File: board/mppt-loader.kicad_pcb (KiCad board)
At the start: 2 copper layers, 102 parts, among them IC101 ATTINY461A-S, IC102 MCP2551-I/SN, P101 CONN_3X2, P102 TST, P103 CONN_11, P104 CONN_11, P105 CONN_5, P106 CONN_4, Q201 IRF 530NS, Q202 IRF 530NS, Q203 IRF 530NS, Q204 IRF 530NS, U101 MCP2515, U102 LD1117-5.0, U201 IR2110, U202 IR2110, U203 LM393, X101 8MHz

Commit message: Finished Schematic and PCB
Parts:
- removed C110, C111: CP, C1V5
- removed U102: LD1117-5.0, SOT223
- added C1: 10u, SM1210, F.Cu at (163.7, 146.0)
- added C2: 10u, SM1210, F.Cu at (163.7, 142.6)
- added C3: 100n, SM0603_Capa, F.Cu at (159.0, 139.8)
- added C4: 10u, SM1210, F.Cu at (168.6, 136.1)
- added C5: 10u, SM1210, F.Cu at (172.0, 136.1)
- added C6: 100n, SM0603_Capa, F.Cu at (171.0, 141.6)
- added C7: 22n, SM0603_Capa, F.Cu at (171.5, 146.8)
- added D1: DIODESCH, DO-214AC(SMA), F.Cu at (164.0, 138.9)
- added F101: FUSE, FUSE5-20, F.Cu at (178.0, 129.1)
- added L1: 22u, SM1210, F.Cu at (163.7, 135.1)
- added R1: 52k3, SM0805, F.Cu at (155.5, 139.1)
- added R2: 10k, SM0805, F.Cu at (155.5, 142.9)
- added R3: 100, SM0805, F.Cu at (175.8, 150.0)
- added R4: 1M, SM0805, F.Cu at (159.2, 146.6)
- added U1: MCP16301, SOT23_6, F.Cu at (159.0, 142.5)
- added U2: LM4132-2.5, SOT23-5, F.Cu at (171.0, 144.2)
- added W102: TEST, PIN_ARRAY_2X1, F.Cu at (165.2, 177.1)
- D102, D103: footprint LED-0805 -> LED-5MM
- D104: value DIODE -> 1N4148; footprint SM1206POL -> sot23
- P103, P104: value CONN_11 -> CONN_12; footprint SIL-12 -> pin_array_6x2
- P105: footprint SIL-5 -> pin_array_3x2
- P106: value CONN_4 -> CONN_8; footprint RIACON_007-4 -> bopla_ak700_8h; moved to B.Cu
- moved C209 177.1 mm to (232.7, 166.7)
- moved C213 176.9 mm to (224.3, 142.2), turned to 180 degrees
- moved C219 174.5 mm to (224.1, 166.9)
- moved Q202 173.5 mm to (223.1, 107.5), turned to 180 degrees
- moved C211 171.2 mm to (232.7, 125.1)
- moved C221 170.7 mm to (224.1, 159.7)
- moved C109 168.7 mm to (177.7, 177.9), turned to 90 degrees
- moved D211 168.0 mm to (229.9, 139.3), turned to 270 degrees
- moved D202 158.0 mm to (205.1, 156.5), turned to 90 degrees
- moved R202 157.7 mm to (223.1, 104.5)
- moved R204 157.6 mm to (223.1, 146.1)
- moved C215 157.2 mm to (228.3, 163.3), turned to 180 degrees
- moved P105 150.0 mm to (172.8, 177.1)
- moved R206 149.4 mm to (200.1, 158.9), turned to 270 degrees
- moved C223 149.2 mm to (219.9, 121.7)
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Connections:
- net N-0000026 renamed /VBAT
- C104 pad 1: N-0000022 (its old number) -> /AVCC
- C107 pad 1: N-0000023 (its old number) -> /VREF
- C203 pad 1: /Powerstage/SENSEA_VOUT -> /Powerstage/VDD_PWR
- C204 pad 1: /Powerstage/SENSEA_VOUT -> /Powerstage/VDD_PWR
- C205 pad 1: /Powerstage/SENSEA_VOUT -> /Powerstage/VDD_PWR
- C206 pad 1: /Powerstage/SENSEA_VOUT -> /Powerstage/VDD_PWR
- C207 pad 2: N-0000074 (its old number) -> /Powerstage/VSA
- C208 pad 2: N-0000066 (its old number) -> /Powerstage/VSB
- C213 pad 2: /Powerstage/SENSEA_VOUT -> /Powerstage/VDD_PWR
- D104 pad 1: /Powerstage/VDD_LOGIC -> +5V
- D104 pad 2: /Powerstage/SENSEA_VOUT -> N-0000032
- D205 pad 1: /Powerstage/SENSEA_VOUT -> /Powerstage/VDD_PWR
- D206 pad 1: /Powerstage/SENSEA_VOUT -> /Powerstage/VDD_PWR
- D207 pad 2: N-0000074 (its old number) -> /Powerstage/VSA
- D208 pad 2: N-0000066 (its old number) -> /Powerstage/VSB
- D209 pad 2: /Powerstage/SENSEA_VOUT -> /Powerstage/VDD_PWR
- D210 pad 2: /Powerstage/SENSEA_VOUT -> /Powerstage/VDD_PWR
- D211 pad 2: /Powerstage/SENSEA_VOUT -> /Powerstage/VDD_PWR
- D212 pad 2: /Powerstage/SENSEA_VOUT -> /Powerstage/VDD_PWR
- IC101 pad 1: N-0000020 (its old number) -> N-0000016
- IC101 pad 15: N-0000022 (its old number) -> /AVCC
- IC101 pad 17: N-0000023 (its old number) -> /VREF
- IC101 pad 19: (no net) -> /CAN_SI
- IC101 pad 2: N-0000011 -> N-0000015
- IC101 pad 3: N-0000019 (its old number) -> N-0000014
- IC101 pad 4: N-0000018 (its old number) -> N-0000013
- IC102 pad 6: N-000008 -> N-0000042
- L101 pad 2: N-0000022 (its old number) -> /AVCC
- L201 pad 1: N-0000074 (its old number) -> /Powerstage/VSA
- L202 pad 1: N-0000066 (its old number) -> /Powerstage/VSB
- P103 pad 10: N-0000019 (its old number) -> N-0000015
- P103 pad 11: N-0000018 (its old number) -> N-0000014
- P103 pad 12: (no net) -> N-0000013
- P103 pad 6: +5V -> /VDDPWR
- P103 pad 7: DGND -> +5V
- P103 pad 8: N-0000020 (its old number) -> DGND
- P103 pad 9: N-0000011 -> N-0000016
- P104 pad 1: /Powerstage/VINA -> /Powerstage/SENSEA_VOUT
- P104 pad 10: /Powerstage/HIGHSIDEB -> /Powerstage/LOWSIDEA
- P104 pad 11: /Powerstage/LOWSIDEB -> /Powerstage/HIGHSIDEB
- P104 pad 12: (no net) -> /Powerstage/LOWSIDEB
- P104 pad 2: /Powerstage/SENSEA_VOUT -> /Powerstage/SENSEA_I
- P104 pad 3: /Powerstage/SENSEA_I -> /Powerstage/SENSEA_VOUT
- P104 pad 4: /Powerstage/SENSEA_VOUT -> /Powerstage/SENSEB_I
- P104 pad 5: /Powerstage/SENSEB_I -> /Powerstage/VINA
- P104 pad 6: /Powerstage/VDD_LOGIC -> /Powerstage/VDD_PWR
- P104 pad 7: /Powerstage/GND_LOGIC -> /Powerstage/VDD_LOGIC
- P104 pad 8: /Powerstage/HIGHSIDEA -> /Powerstage/GND_LOGIC
- P104 pad 9: /Powerstage/LOWSIDEA -> /Powerstage/HIGHSIDEA
- P105 pad 1: (no net) -> N-0000027
- P105 pad 4: N-000008 -> N-0000042
- P106 pad 1: /Powerstage/VINA -> /Powerstage/GND_LOGIC
- P106 pad 4: /Powerstage/GND_LOGIC -> /Powerstage/SENSEA_VOUT
- Q201 pad S: N-0000074 (its old number) -> /Powerstage/VSA
- Q202 pad D: N-0000074 (its old number) -> /Powerstage/VSA
- Q203 pad S: N-0000066 (its old number) -> /Powerstage/VSB
- Q204 pad D: N-0000066 (its old number) -> /Powerstage/VSB
- R116 pad 2: N-000007 -> N-0000041
- U101 pad 14: (no net) -> /CAN_SI
- U201 pad 3: /Powerstage/SENSEA_VOUT -> /Powerstage/VDD_PWR
- U201 pad 5: N-0000074 (its old number) -> /Powerstage/VSA
- U202 pad 3: /Powerstage/SENSEA_VOUT -> /Powerstage/VDD_PWR
- U202 pad 5: N-0000066 (its old number) -> /Powerstage/VSB
- U203 pad 8: /Powerstage/SENSEA_VOUT -> /Powerstage/VDD_PWR
- W101 pad 1: N-000007 -> N-0000027
- W101 pad 2: N-000008 -> +5V
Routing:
- net +5V: track 0.00 -> 210.4 mm, vias 0 -> 7
- net /Powerstage/GND_LOGIC: track 0.00 -> 205.6 mm, vias 0 -> 58
- net /Powerstage/VINA: track 0.00 -> 126.5 mm, vias 0 -> 28
- net /Powerstage/VDD_PWR: track 0.00 -> 97.9 mm
- net DGND: track 0.00 -> 93.0 mm, vias 0 -> 17
- net /Powerstage/SENSEA_VOUT: track 0.00 -> 87.9 mm, vias 0 -> 22
- net /Powerstage/VSB: track 0.00 -> 85.5 mm, vias 0 -> 20
- net /Powerstage/VSA: track 0.00 -> 76.6 mm, vias 0 -> 20
- net /Powerstage/VDD_LOGIC: track 0.00 -> 63.4 mm, vias 0 -> 4
- net /VDDPWR: track 0.00 -> 50.1 mm, vias 0 -> 2
- net /Powerstage/SENSEB_I: track 0.00 -> 48.9 mm, vias 0 -> 1
- net /Powerstage/LOWSIDEA: track 0.00 -> 46.1 mm
- net N-0000068: track 0.00 -> 42.8 mm, vias 0 -> 2
- net N-0000066: track 0.00 -> 40.2 mm, vias 0 -> 2
- net /RESET: track 0.00 -> 39.5 mm, vias 0 -> 2
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- added copper zone on F.Cu, net +5V
- added copper zone on B.Cu, net /Powerstage/GND_LOGIC
- added copper zone on F.Cu, net /Powerstage/GND_LOGIC
- added copper zone on F.Cu, net /Powerstage/SENSEA_I
- added copper zone on B.Cu, net /Powerstage/SENSEA_VOUT
- added copper zone on F.Cu, net /Powerstage/SENSEA_VOUT
- added copper zone on F.Cu, net /Powerstage/SENSEB_I
- added copper zone on B.Cu, net /Powerstage/VINA
- added copper zone on F.Cu, net /Powerstage/VINA
- added copper zone on B.Cu, net /Powerstage/VSA
- added copper zone on F.Cu, net /Powerstage/VSA
- added copper zone on B.Cu, net /Powerstage/VSB
- added copper zone on F.Cu, net /Powerstage/VSB
- added copper zone on F.Cu, net /VDDPWR
- added copper zone on B.Cu, net DGND
- added copper zone on F.Cu, net DGND
- added copper zone on F.Cu, net N-0000031
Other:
- board outline added: 84 x 78.7 mm
- net class Default: clearance 0.254 -> 0.2; via_dia 0.889 -> 0.8; via_drill 0.635 -> 0.3
- rule pad_to_mask_clearance: 0 -> 0.15
- rule trace_clearance: 0.254 -> 0.2
- rule trace_min: 0.254 -> 0.15
- rule via_min_drill: 0.508 -> 0.3
- rule via_min_size: 0.889 -> 0.5

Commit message: Workaround segmentation fault of Kicad
* Slightly increase Mask-Pad Offset to work around
  segementation fault when exporting gerber front mask
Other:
- rule pad_to_mask_clearance: 0.15 -> 0.2
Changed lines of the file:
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@@
-(kicad_pcb (version 3) (host pcbnew "(2013-may-01)-stable")
+(kicad_pcb (version 3) (host pcbnew "(2013-jul-07)-stable")
   (general
     (links 259)
     (no_connects 2)
-    (area 152.224999 102.024999 240.975001 180.875001)
+    (area 152.038889 101.999999 236.972222 195.875001)
     (thickness 1.6)
     (drawings 15)
@@
   )
   (setup
-    (last_trace_width 1)
+    (last_trace_width 0.254)
     (user_trace_width 0.5)
     (user_trace_width 0.75)
@@
     (pad_size 3.6576 2.032)
     (pad_drill 0)
-    (pad_to_mask_clearance 0.15)
+    (pad_to_mask_clearance 0.2)
     (solder_mask_min_width 0.15)
     (aux_axis_origin 0 0)
     (visible_elements 7FFFFFBF)
     (pcbplotparams
-      (layerselection 3178497)
+      (layerselection 15761409)
       (usegerberextensions true)
       (excludeedgelayer true)
-      (linewidth 0)
+      (linewidth 0.150000)
       (plotframeref false)
       (viasonmask false)
@@
       (outputformat 1)
       (mirror false)
-      (drillshape 1)
+      (drillshape 0)
       (scaleselection 1)
-      (outputdirectory ""))
+      (outputdirectory /tmp))
   )
   (net 0 "")

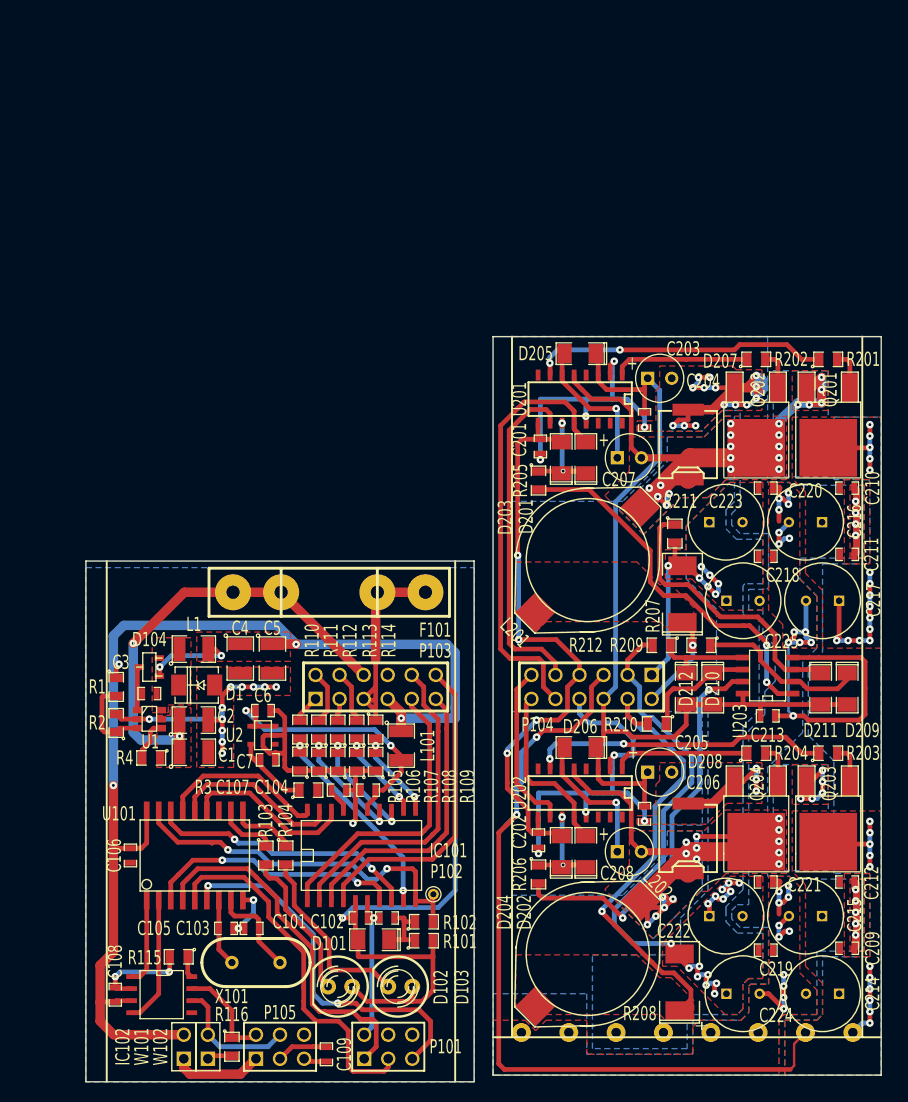
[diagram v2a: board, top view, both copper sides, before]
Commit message: Fix wrong connections of PWM and ADC
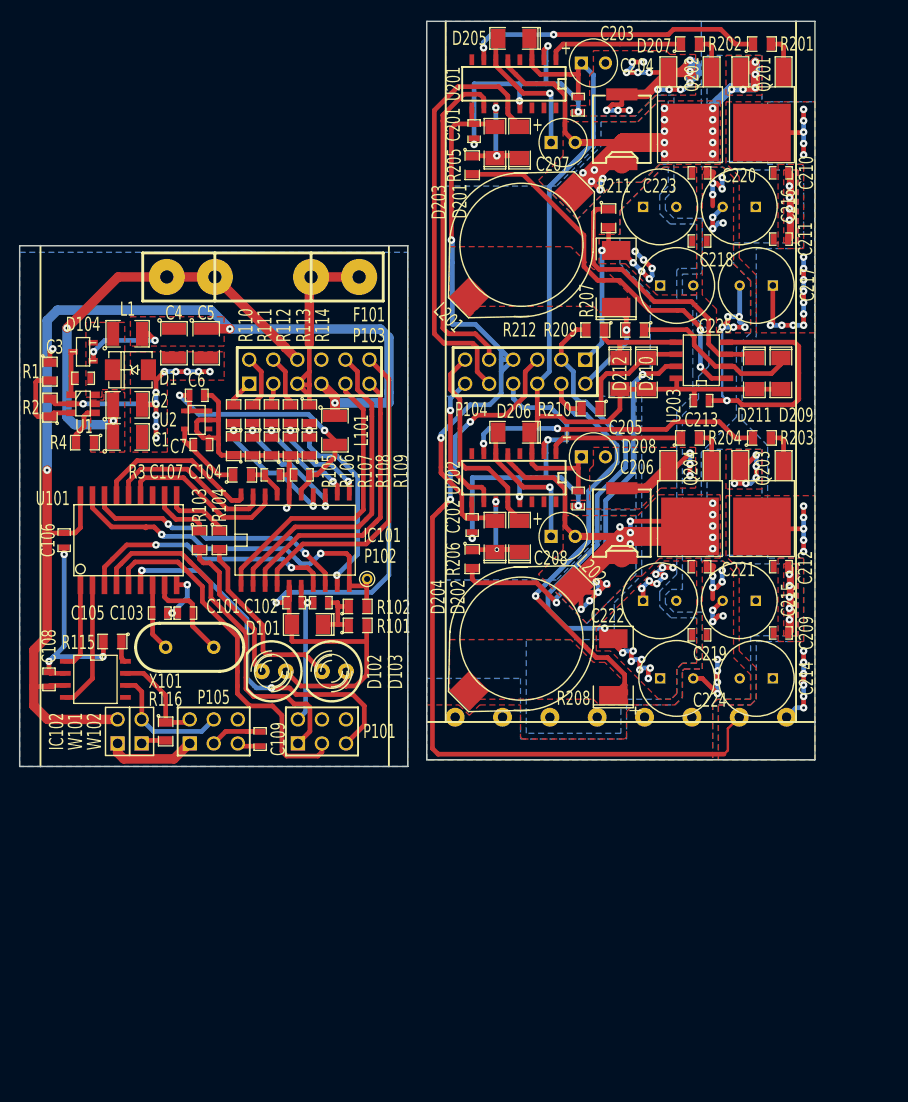
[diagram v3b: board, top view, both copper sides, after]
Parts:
- Q201, Q202, Q203, Q204: value IRF 530NS -> IRLU024N
- moved C101 34.0 mm to (174.3, 130.2)
- moved C102 34.0 mm to (177.1, 130.2)
- moved C106 34.0 mm to (150.0, 123.6)
- moved C109 34.0 mm to (170.7, 144.6)
- moved C202 34.0 mm to (193.1, 122.0)
- moved C204 34.0 mm to (204.3, 77.6)
- moved C207 34.0 mm to (202.7, 81.6)
- moved C213 34.0 mm to (217.3, 108.9)
- moved C214 34.0 mm to (223.1, 138.2)
- moved C215 34.0 mm to (221.3, 130.0)
- moved C219 34.0 mm to (217.1, 133.6)
- moved C222 34.0 mm to (212.9, 130.0)
- moved C224 34.0 mm to (214.7, 138.2)
- moved C3 34.0 mm to (152.0, 106.5)
- moved C7 34.0 mm to (164.5, 113.5)
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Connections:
- IC101 pad 11: N-0000018 (its old number) -> N-0000023
- IC101 pad 12: N-0000017 (its old number) -> N-0000022
- IC101 pad 13: N-0000019 (its old number) -> N-0000021
- IC101 pad 14: N-0000024 -> N-0000056
- IC101 pad 9: N-0000056 -> N-0000015
- P104 pad 11: /Powerstage/HIGHSIDEB -> /Powerstage/LOWSIDEB
- P104 pad 12: /Powerstage/LOWSIDEB -> /Powerstage/HIGHSIDEB
- R106 pad 2: N-0000024 -> N-0000021
- R107 pad 2: N-0000019 (its old number) -> N-0000022
- R108 pad 2: N-0000017 (its old number) -> N-0000023
- R109 pad 2: N-0000018 (its old number) -> N-0000015
- R111 pad 1: N-0000024 -> N-0000021
- R112 pad 1: N-0000019 (its old number) -> N-0000022
- R113 pad 1: N-0000017 (its old number) -> N-0000023
- R114 pad 2: N-0000018 (its old number) -> N-0000015
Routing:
- net N-0000015: track 0.00 -> 22.1 mm, vias 0 -> 2
- net N-0000021: track 0.00 -> 14.4 mm, vias 0 -> 2
- net N-0000024: track 13.4 -> 0.00 mm, vias 2 -> 0
- net N-0000019 (its old number): track 13.1 -> 0.00 mm, vias 2 -> 0
- net DGND: track 93.0 -> 105.7 mm, vias 17 -> 18
- net N-0000022: track 0.00 -> 12.0 mm, vias 0 -> 2
- net N-0000023: track 0.00 -> 11.8 mm, vias 0 -> 2
- net N-0000017 (its old number): track 10.3 -> 0.00 mm, vias 2 -> 0
- net N-0000018 (its old number): track 10.0 -> 0.00 mm, vias 2 -> 0
- net N-0000056: track 22.4 -> 14.9 mm
- net /Powerstage/LOWSIDEB: track 18.7 -> 22.1 mm
- net /Powerstage/VDD_LOGIC: track 63.4 -> 66.1 mm, vias 4 -> 2
- net /Powerstage/HIGHSIDEB: track 17.9 -> 15.3 mm, vias 0 -> 1
- net /Powerstage/VINA: track 126.5 -> 124.8 mm
- net /VREF: track 2.59 -> 4.08 mm
